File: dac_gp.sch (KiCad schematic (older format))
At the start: 48 parts, among them U1 DAC80508ZRTER, U2 OPA2156xD, U3 OPA2156xD, U4 OPA2156xD, U6 OPA2156xD, U7 TMUX6136PWR, U9 TMUX6136PWR

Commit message: updates to gp ADC
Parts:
- gave numbers to parts that had none: 24

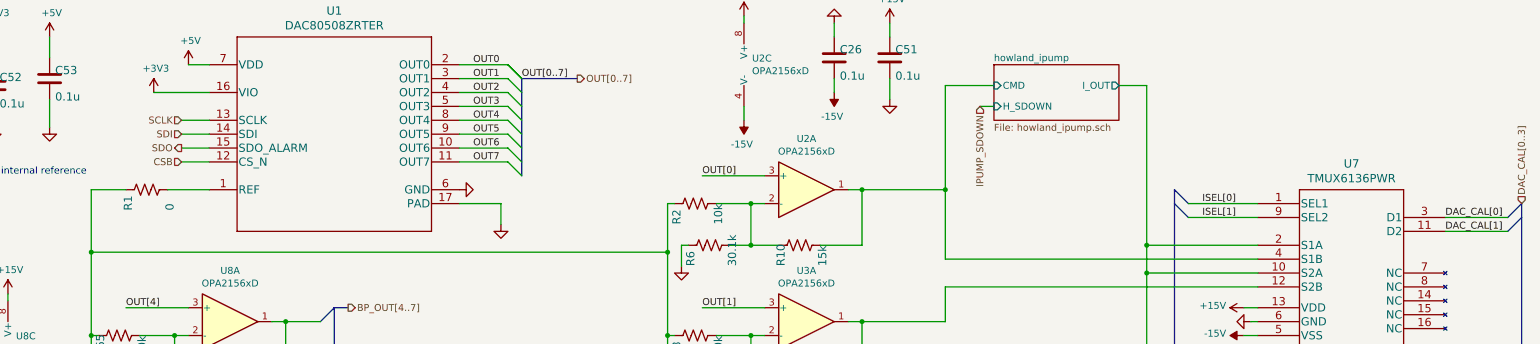
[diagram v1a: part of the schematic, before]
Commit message: moved level shifters to FPGA
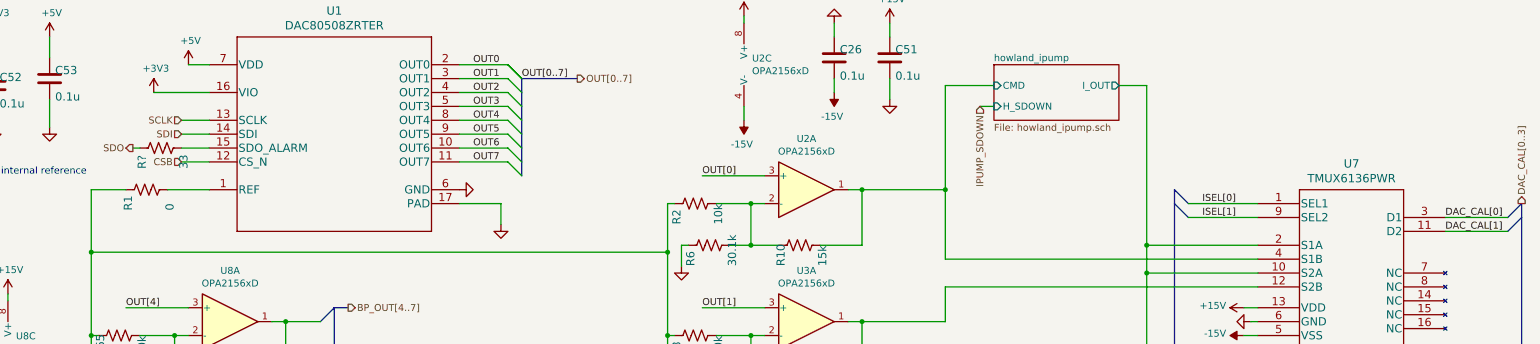
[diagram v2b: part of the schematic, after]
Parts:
- added R?: 33, Resistor_SMD:R_0603_1608Metric, symbol Device:R_US
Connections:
- wire segments 194 -> 195
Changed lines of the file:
@@
 Text HLabel 2000 1600 0    50   Input ~ 0
 SDI
-Text HLabel 2000 1700 0    50   Output ~ 0
+Text HLabel 1650 1700 0    50   Output ~ 0
 SDO
 Text HLabel 2000 1800 0    50   Input ~ 0
@@
 	5500 3050 5500 5250
 Connection ~ 5500 5250
-Text HLabel 11650 2100 1    50   Input ~ 0
+Text HLabel 11650 2100 1    50   Output ~ 0
 DAC_CAL[0..3]
 Text HLabel 9150 3450 2    50   Input ~ 0
@@
 Wire Wire Line
 	7500 2000 7500 1250
+$Comp
+L Device:R_US R?
+U 1 1 617C87E1
+P 1850 1700
+AR Path="/6095A38A/617C87E1" Ref="R?"  Part="1"
+AR Path="/6095BD4C/617C87E1" Ref="R?"  Part="1"
+F 0 "R?" H 1700 1800 59  0000 L BNN
+F 1 "33" H 1700 1500 59  0000 L BNN
+F 2 "Resistor_SMD:R_0603_1608Metric" H 1850 1700 50  0001 C CNN
+F 3 "" H 1850 1700 50  0001 C CNN
+	1    1850 1700
+	0    -1   -1   0
+$EndComp
+Wire Wire Line
+	1700 1700 1650 1700
 Wire Bus Line
 	9150 2000 9150 5250

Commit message: updates to high-speed DAC
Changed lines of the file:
@@
 AR Path="/6095BD4C/617C87E1" Ref="R?"  Part="1"
 F 0 "R?" H 1700 1800 59  0000 L BNN
-F 1 "33" H 1700 1500 59  0000 L BNN
+F 1 "33" H 1900 1800 59  0000 L BNN
 F 2 "Resistor_SMD:R_0603_1608Metric" H 1850 1700 50  0001 C CNN
 F 3 "" H 1850 1700 50  0001 C CNN

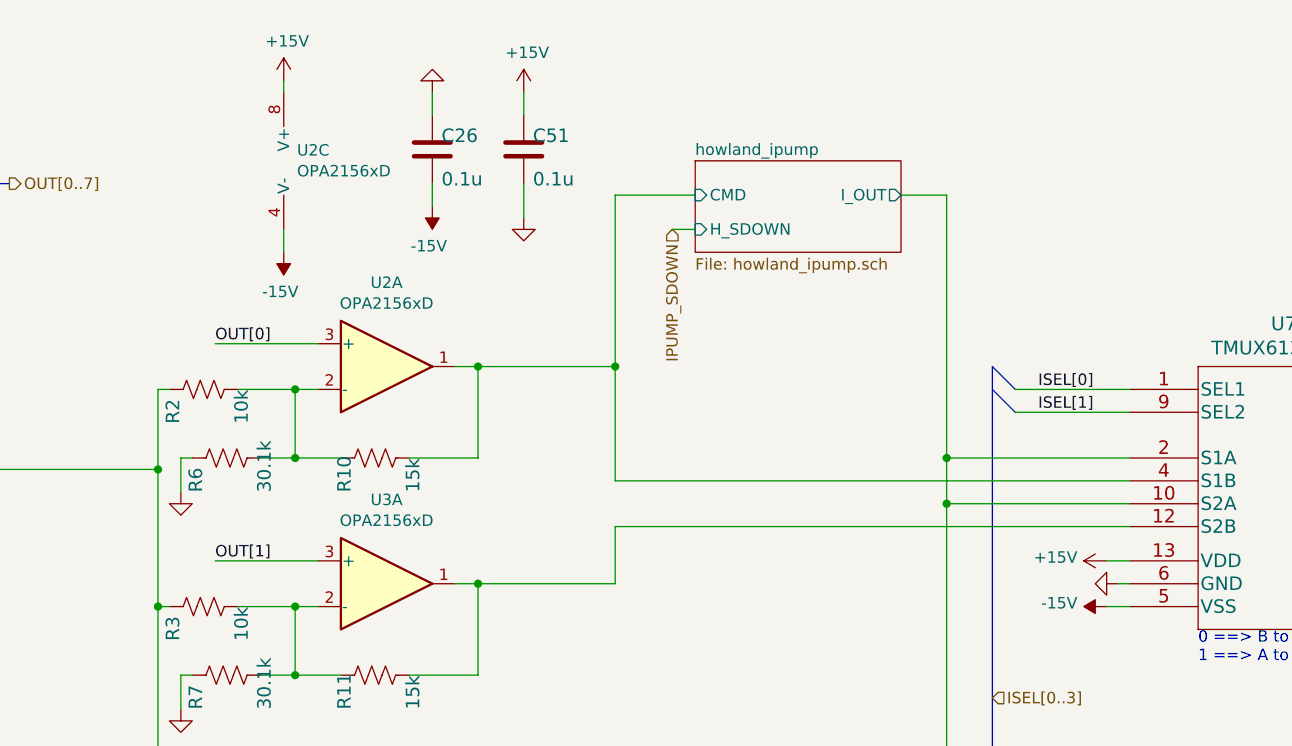
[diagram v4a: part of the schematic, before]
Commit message: near complete top level schematic routing
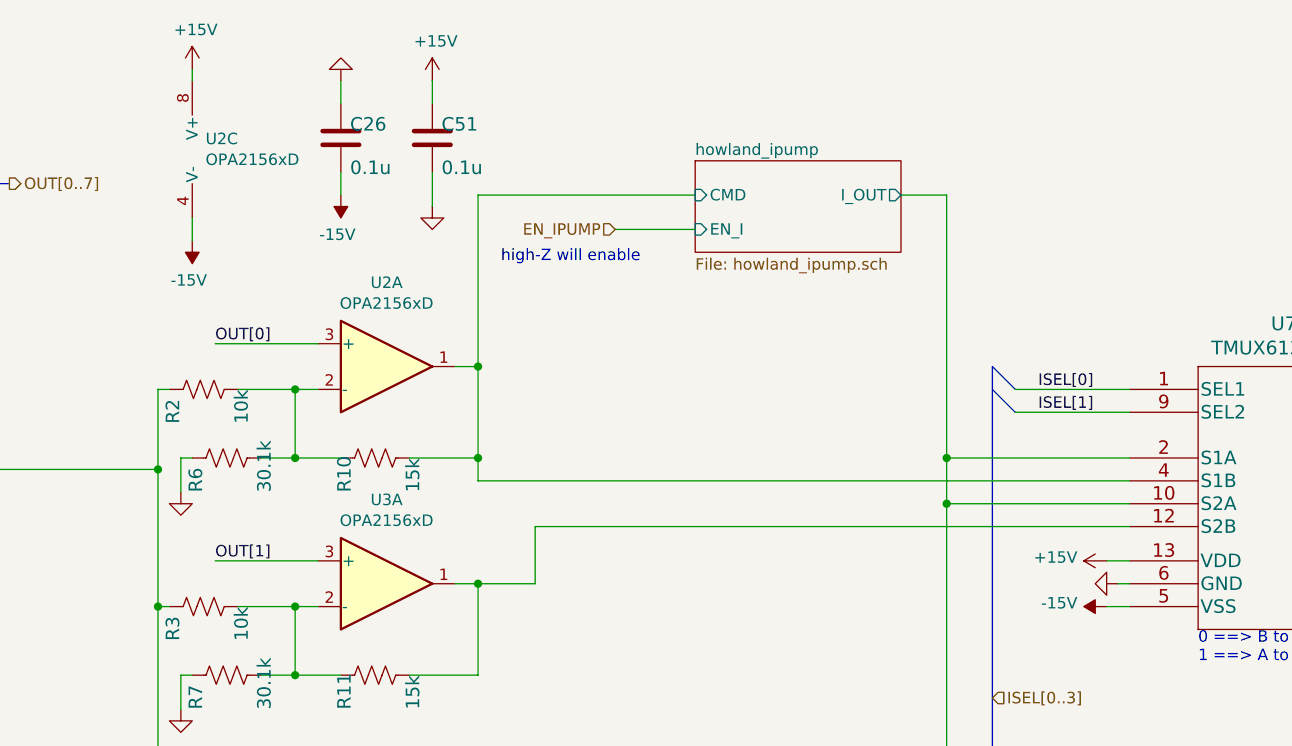
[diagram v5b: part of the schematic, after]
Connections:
- net labels added: EN_IPUMP
- net labels removed: IPUMP_SDOWN
- wire segments 195 -> 194
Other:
- note added: "high-Z will enable"
- moved on the sheet: C26, C51, U2C

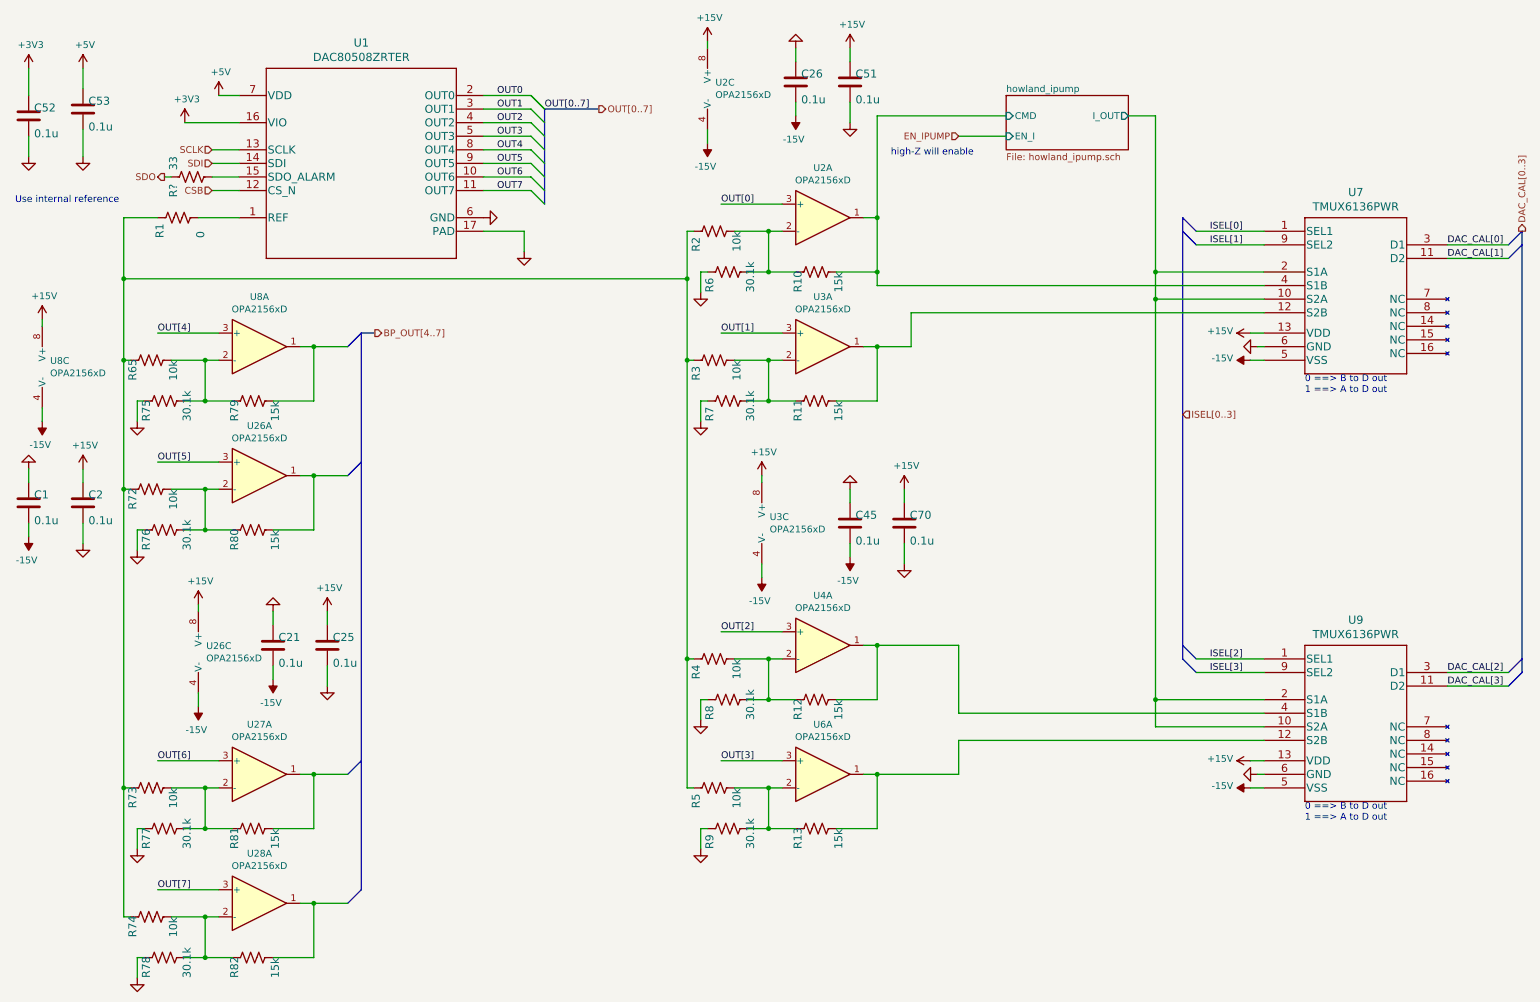
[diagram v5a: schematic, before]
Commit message: corrected most ERC errors
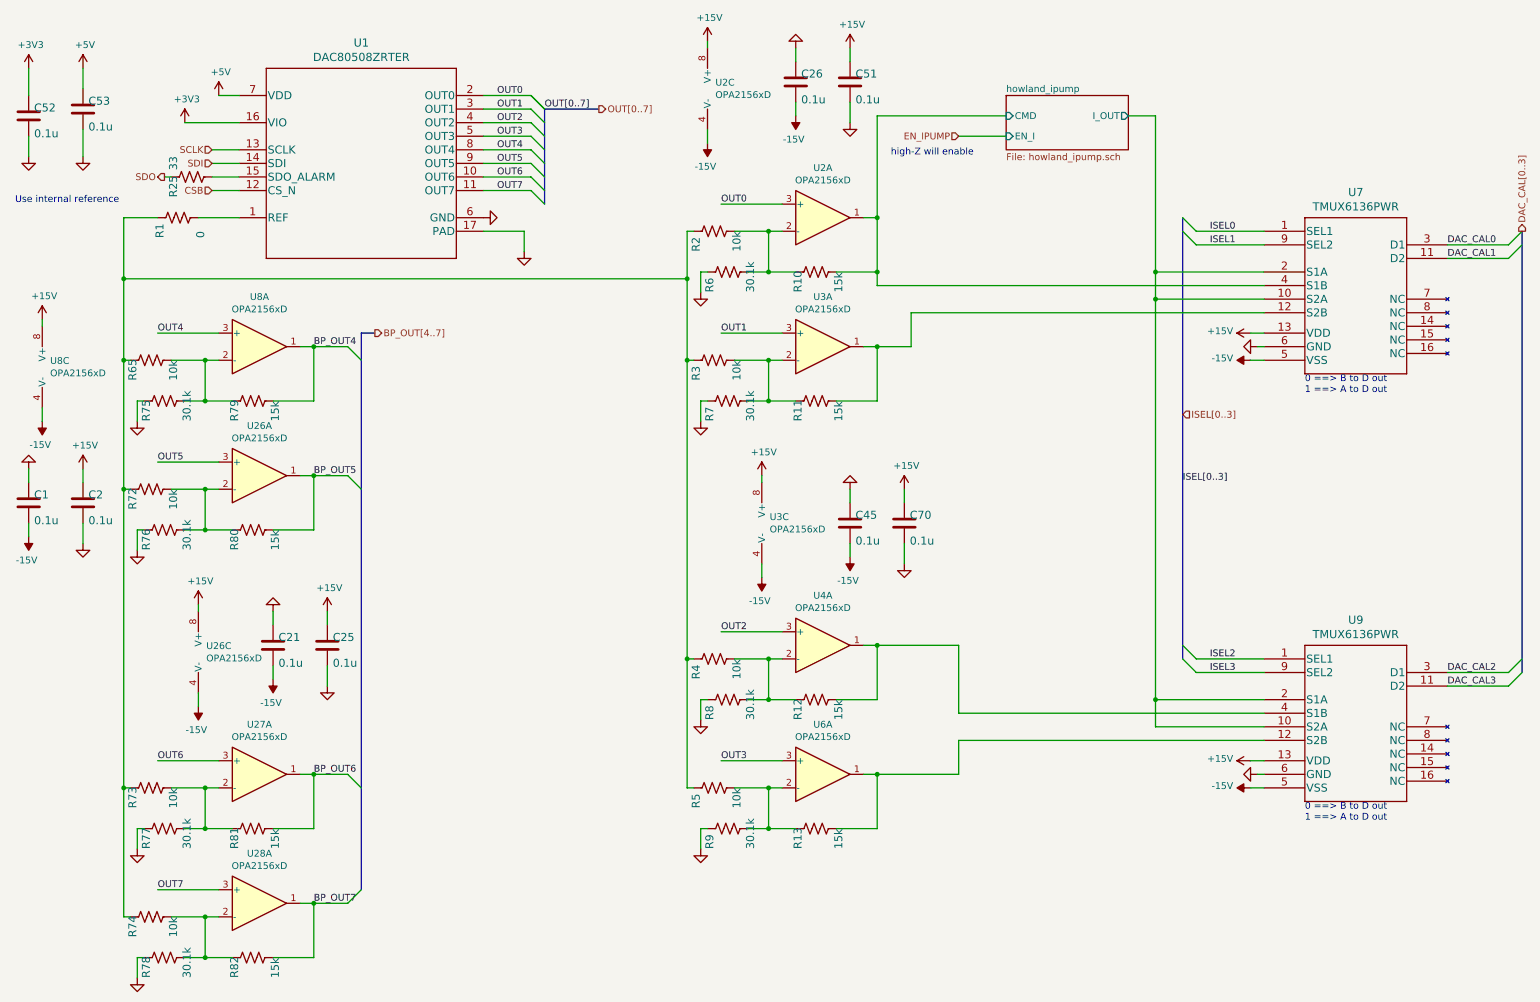
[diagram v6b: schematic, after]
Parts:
- gave numbers to parts that had none: 1
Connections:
- net labels added: BP_OUT4, BP_OUT5, BP_OUT6, BP_OUT7, DAC_CAL0, DAC_CAL1, DAC_CAL2, DAC_CAL3, ISEL0, ISEL1, ISEL2, ISEL3
- net labels removed: DAC_CAL[0], DAC_CAL[1], DAC_CAL[2], DAC_CAL[3], ISEL[0], ISEL[1], ISEL[2], ISEL[3], OUT[0], OUT[1], OUT[2], OUT[3], OUT[4], OUT[5], OUT[6], OUT[7]

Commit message: after using kifield to update Manf#
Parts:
- C1, C2, C21, C25, C26, C45, C51, C52, C53, C70: Manufacturer_Name (none) -> Yageo; Tolerance (none) -> 20%; voltage (none) -> 25
- R1: Manf# (none) -> RC0603FR-070RL; Power (none) -> 0.1W
- R2, R3, R4, R5, R6, R65, R7, R72, R73, R74, R75, R76, R77, R78, R8, R80, R81, R82, R9: Power (none) -> 0.1W; Tolerance (none) -> 1%
- R25: Manf# (none) -> RC0603FR-0733RL; Power (none) -> 0.1W; Tolerance (none) -> 1%
- U1: Alternate (none) -> DAC80508MCRTET; Manf# (none) -> DAC80508ZCRTET
- U2, U26, U27, U28, U3, U4, U6, U8: Manf# (none) -> OPA2156IDR
- U7, U9: footprint PW16_TEX -> digikey-footprints:TSSOP-16_W4.4mm; Manf# (none) -> TMUX6136PWR

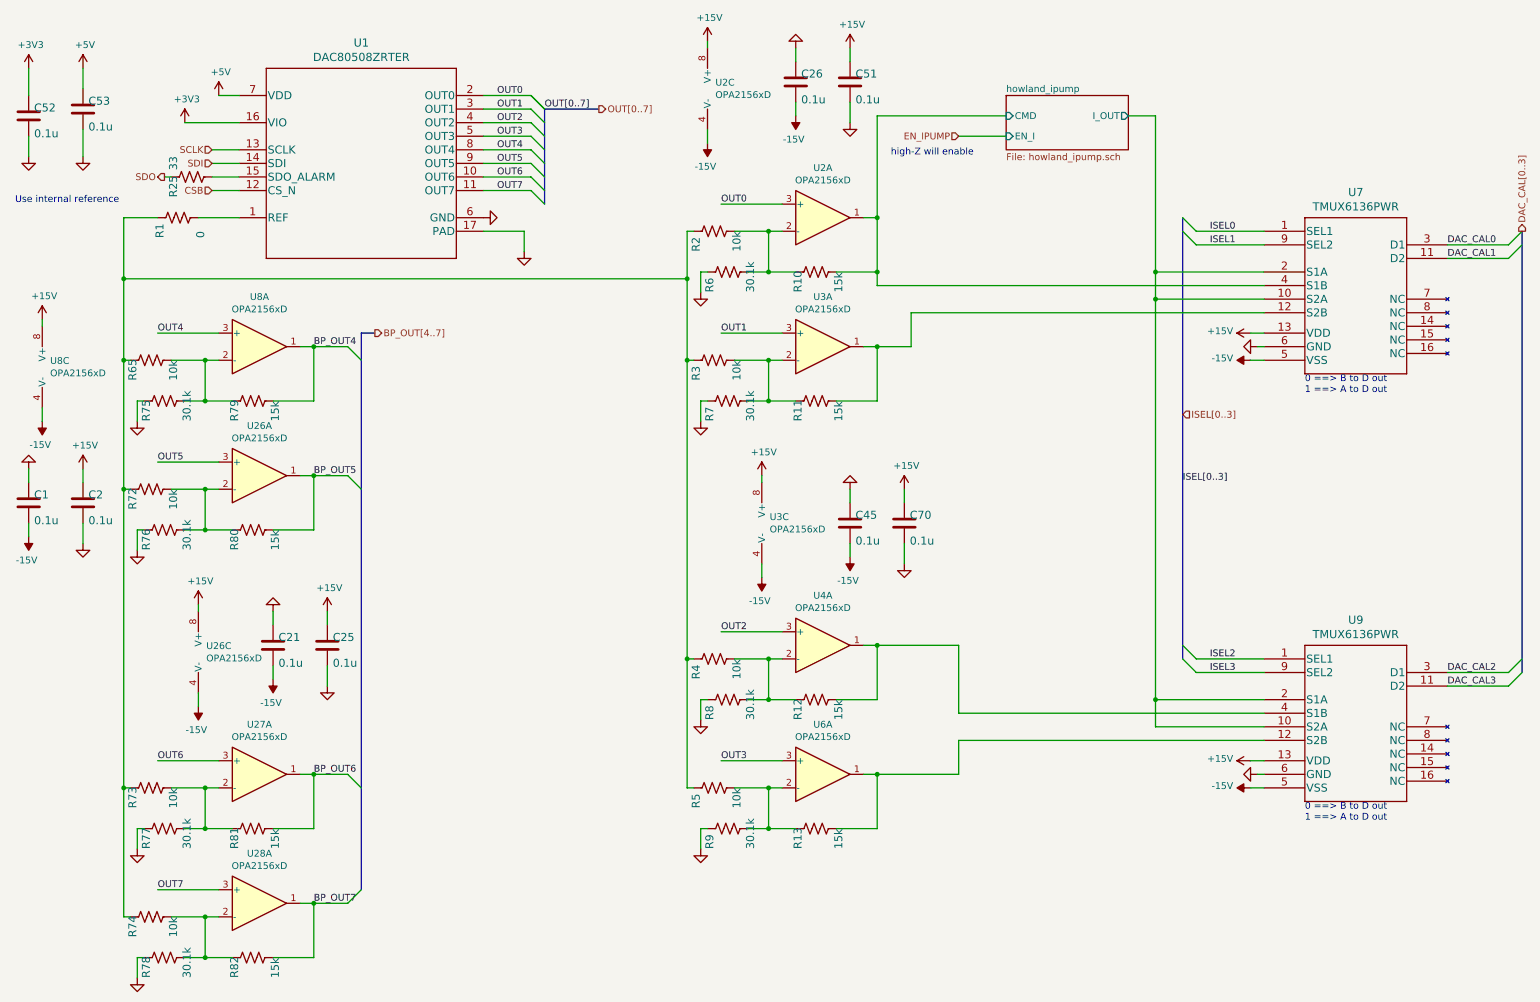
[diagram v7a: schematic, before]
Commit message: changed 0.1uF cap to Samsung
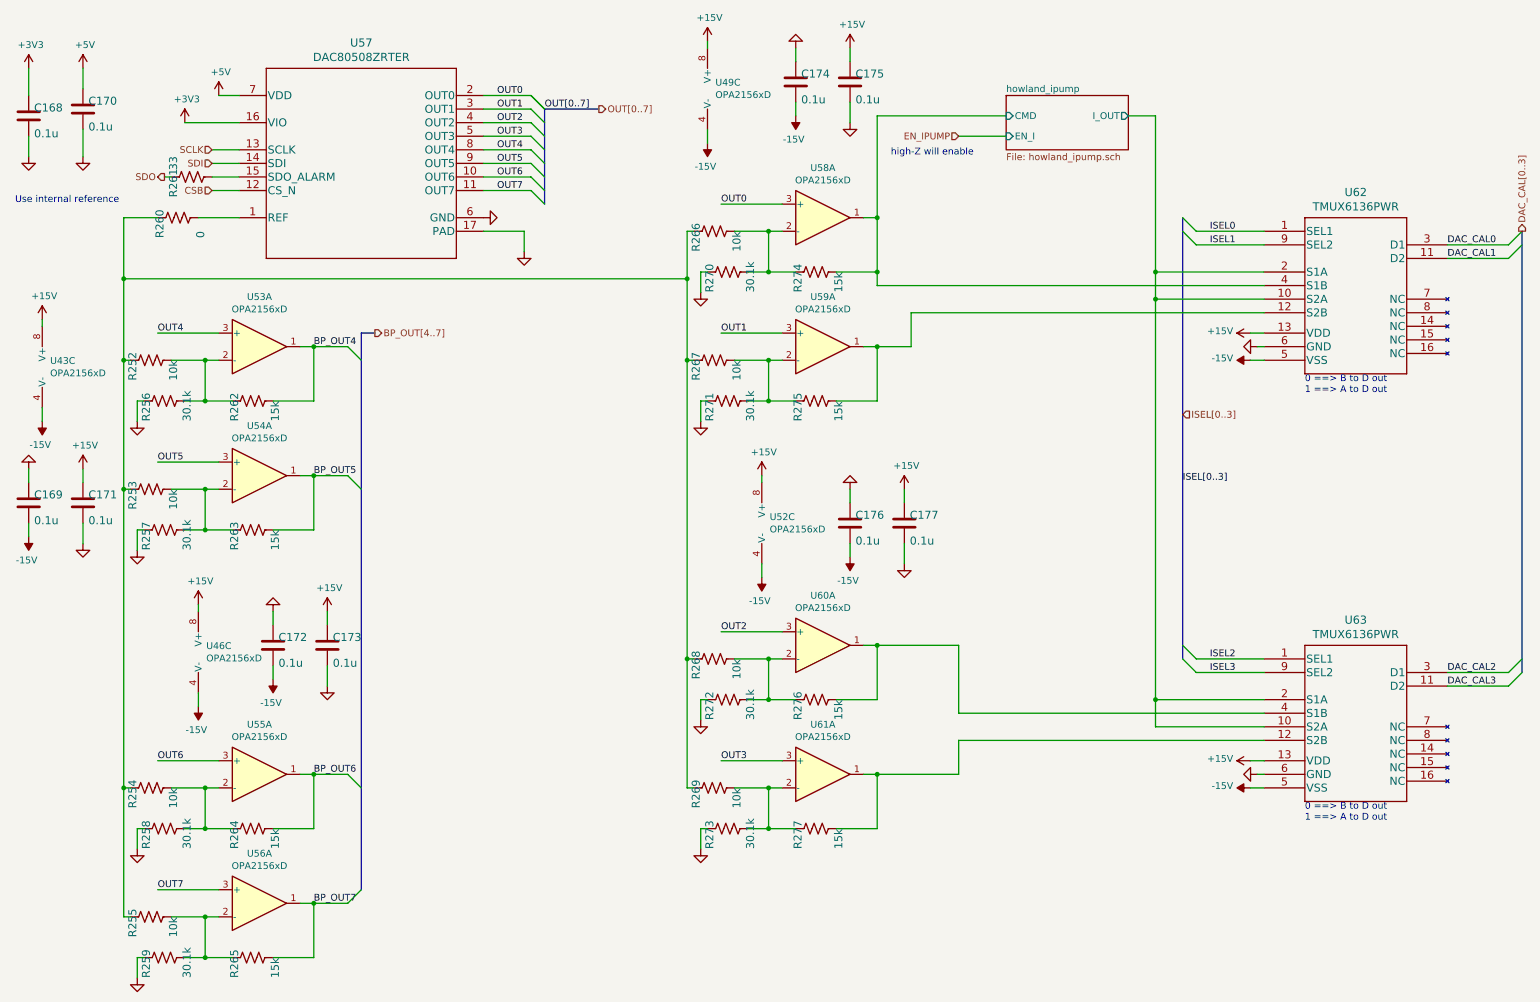
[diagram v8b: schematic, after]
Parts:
- U1: footprint RTE0016D -> Package_DFN_QFN:WQFN-16-1EP_3x3mm_P0.5mm_EP1.6x1.6mm
- U7, U9: footprint digikey-footprints:TSSOP-16_W4.4mm -> Package_SO:TSSOP-16_4.4x5mm_P0.65mm
